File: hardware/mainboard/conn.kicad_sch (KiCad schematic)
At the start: 25 parts

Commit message: Connecting up various bits
Signed-off-by: David Shah <dave@ds0.me>
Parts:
- removed C? (x4): 10µ, symbol Device:C_Small
- removed C? (x8): 470n, symbol Device:C_Small
- removed R? (x5): 4.7k, symbol Device:R_Small
- removed U? (x8): LIFCL_40_CABGA400, symbol meowality:LIFCL_40_CABGA400
- added C? (x4): 100n, symbol Device:C_Small
- added C? (x2): 10µ, symbol Device:C_Small
- added C?: 2.2µ, symbol Device:C_Small
- added FB? (x3): 120, symbol Device:FerriteBead_Small
- added P?: M2_SOCKET_E, symbol meowality:M2_SOCKET_E
- added R?: 1.15k, symbol Device:R_Small
- added R?: 10k, symbol Device:R_Small
- added U?: LIFCL_40_CABGA400, symbol meowality:LIFCL_40_CABGA400
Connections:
- net +1V8: now also FB?.2, FB?.2
- net +3V3: now also P?.2 (3.3V), P?.4 (3.3V), P?.72 (3.3V), P?.74 (3.3V), R?.1
- net GND: now also C?.2, C?.2, C?.2, C?.2, C?.2, P?.1 (GND), P?.18 (GND), P?.33 (GND), P?.39 (GND), P?.45 (GND), P?.51 (GND), P?.57 (GND), P?.63 (GND), P?.69 (GND), P?.7 (GND), P?.75 (GND)
- new net: C?.1, C?.1, C?.1, FB?.1, U?.B13 (VCCSD0), U?.B15 (VCCSD0)
- new net: C?.1, C?.1, FB?.1, U?.B11 (VCCAUXSD)
- new net: C?.2, C?.2, FB?.1, U?.C13 (VCCPLLSD0)
- new net: R?.1, U?.C14 (SD0_REXT)
- new net: P?.55 (~PEWAKE0), R?.2
- new net +1V0: FB?.2
- new net M2_DISABLE1: P?.56 (W_DISABLE1)
- new net M2_DISABLE2: P?.54 (W_DISABLE2)
- new net M2_REFCLK0+: P?.47 (REFCLK0+)
- new net M2_REFCLK0-: P?.49 (REFCLK0-)
- new net M2_RX0+: P?.35 (PER0+), U?.A13 (SD0_TXDP/+)
- new net M2_RX0-: P?.37 (PER0-), U?.A12 (SD0_TXDN/-)
- new net M2_SDIO_CLK: P?.9 (SDIO_CLK)
- new net M2_SDIO_CMD: P?.11 (SDIO_CMD)
- new net M2_SDIO_D0: P?.13 (SDIO_D0)
- new net M2_SDIO_D1: P?.15 (SDIO_D1)
- new net M2_SDIO_D2: P?.17 (SDIO_D2)
- new net M2_SDIO_D3: P?.19 (SDIO_D3)
- new net M2_SDIO_~RESET: P?.23 (SDIO_~RESET)
- new net M2_SDIO_~WAKE: P?.21 (SDIO_~WAKE)
- new net M2_TX0+: P?.41 (PET0+), U?.A16 (SD0_RXDP/+)
- new net M2_TX0-: P?.43 (PET0-), U?.A15 (SD0_RXDN/-)
- new net M2_~RST: P?.52 (~PERST0)
- new net SD0_REFRET: C?.1, C?.1, R?.2, U?.B14 (SD0_REFRET)
- no-connect marks 0 -> 25
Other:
- note added: "1.15k --> 100Ω diff"
- note added: "Double check direction!!"

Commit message: Misc bits
Signed-off-by: David Shah <dave@ds0.me>
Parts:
- added J? (x2): Conn_01x40_Shielded, symbol Connector_Generic_Shielded:Conn_01x40_Shielded
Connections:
- net +3V3: now also J?.37 (Pin_37), J?.37 (Pin_37), J?.38 (Pin_38), J?.38 (Pin_38), J?.39 (Pin_39), J?.39 (Pin_39), J?.40 (Pin_40), J?.40 (Pin_40)
- net GND: now also J?.1 (Pin_1), J?.1 (Pin_1), J?.10 (Pin_10), J?.10 (Pin_10), J?.13 (Pin_13), J?.13 (Pin_13), J?.16 (Pin_16), J?.16 (Pin_16), J?.19 (Pin_19), J?.19 (Pin_19), J?.22 (Pin_22), J?.22 (Pin_22), J?.25 (Pin_25), J?.25 (Pin_25), J?.30 (Pin_30), J?.30 (Pin_30), J?.35 (Pin_35), J?.35 (Pin_35), J?.4 (Pin_4), J?.4 (Pin_4), J?.7 (Pin_7), J?.7 (Pin_7)
- new net B2BL_CLKI+: J?.2 (Pin_2)
- new net B2BL_CLKI-: J?.3 (Pin_3)
- new net B2BL_CLKO+: J?.8 (Pin_8)
- new net B2BL_CLKO-: J?.9 (Pin_9)
- new net B2BL_DI0+: J?.5 (Pin_5)
- new net B2BL_DI0-: J?.6 (Pin_6)
- new net B2BL_DI1+: J?.11 (Pin_11)
- new net B2BL_DI1-: J?.12 (Pin_12)
- new net B2BL_DI2+: J?.14 (Pin_14)
- new net B2BL_DI2-: J?.15 (Pin_15)
- new net B2BL_DO0+: J?.17 (Pin_17)
- new net B2BL_DO0-: J?.18 (Pin_18)
- new net B2BL_DO1+: J?.20 (Pin_20)
- new net B2BL_DO1-: J?.21 (Pin_21)
- new net B2BL_DO2+: J?.23 (Pin_23)
- new net B2BL_DO2-: J?.24 (Pin_24)
- new net B2BL_MISC0: J?.31 (Pin_31)
- new net B2BL_MISC1: J?.32 (Pin_32)
- new net B2BL_MISC2: J?.33 (Pin_33)
- new net B2BR_CLKI+: J?.14 (Pin_14), J?.8 (Pin_8)
- new net B2BR_CLKI-: J?.9 (Pin_9)
- new net B2BR_CLKO+: J?.2 (Pin_2)
- new net B2BR_CLKO-: J?.3 (Pin_3)
- new net B2BR_DI0+: J?.17 (Pin_17)
- new net B2BR_DI0-: J?.18 (Pin_18)
- new net B2BR_DI1+: J?.20 (Pin_20)
- new net B2BR_DI1-: J?.21 (Pin_21)
- new net B2BR_DI2+: J?.23 (Pin_23)
- new net B2BR_DI2-: J?.24 (Pin_24)
- new net B2BR_DO0+: J?.5 (Pin_5)
- new net B2BR_DO0-: J?.6 (Pin_6)
- new net B2BR_DO1+: J?.11 (Pin_11)
- new net B2BR_DO1-: J?.12 (Pin_12)
- new net B2BR_DO2-: J?.15 (Pin_15)
- new net B2BR_MISC0: J?.31 (Pin_31)
- new net B2BR_MISC1: J?.32 (Pin_32)
- new net B2BR_MISC2: J?.33 (Pin_33)
- new net JTAG_TCK: J?.27 (Pin_27), J?.27 (Pin_27)
- new net JTAG_TDI_L: J?.28 (Pin_28)
- new net JTAG_TDI_R: J?.28 (Pin_28)
- new net JTAG_TDO_L: J?.29 (Pin_29)
- new net JTAG_TDO_R: J?.29 (Pin_29)
- new net JTAG_TMS: J?.26 (Pin_26), J?.26 (Pin_26)
- new net PRES_L: J?.34 (Pin_34)
- new net PRES_R: J?.34 (Pin_34)
- no-connect marks 25 -> 27

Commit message: More stuff
Signed-off-by: David Shah <dave@ds0.me>
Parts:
- added C? (x2): 12p, symbol Device:C_Small
- added C? (x2): 470n, symbol Device:C_Small
- added FB?: 120R, symbol Device:FerriteBead_Small
- added J?: EAR, symbol Connector_Generic:Conn_01x06
- added R?: 10k, symbol Device:R_Small
- added U?: Si52112-B, symbol meowality:Si52112-B
- added U?: 74AHC1G126, symbol 74xGxx:74AHC1G126
- added Y?: 25MHz, symbol Device:Crystal_GND3_Small
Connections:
- net JTAG_TDO_R is gone; now on net JTAG_TDO_L: J?.29 (Pin_29)
- net +3V3: now also FB?.1, J?.1 (Pin_1), R?.2, U?.5 (VCC)
- net GND: now also J?.34 (Pin_34), C?.2, C?.2, C?.2, C?.2, J?.6 (Pin_6), U?.3 (GND), U?.4 (Vss), U?.5 (Vss), Y?.3; no longer J?.35 (Pin_35)
- net JTAG_TDI_R: now also U?.2
- net JTAG_TDO_L: now also U?.4
- net M2_REFCLK0+: now also U?.6 (DIFF1+)
- net M2_REFCLK0-: now also U?.7 (DIFF1-)
- net PRES_R: now also J?.35 (Pin_35), R?.1, U?.1; no longer J?.34 (Pin_34)
- net JTAG_TDI_L renamed JTAG_TDI
- net M2_SDIO_CLK: no longer names the net of P?.9 (SDIO_CLK)
- net M2_SDIO_CMD: no longer names the net of P?.11 (SDIO_CMD)
- net M2_SDIO_D0: no longer names the net of P?.13 (SDIO_D0)
- net M2_SDIO_D1: no longer names the net of P?.15 (SDIO_D1)
- net M2_SDIO_D2: no longer names the net of P?.17 (SDIO_D2)
- net M2_SDIO_D3: no longer names the net of P?.19 (SDIO_D3)
- net M2_SDIO_~RESET: no longer names the net of P?.23 (SDIO_~RESET)
- net M2_SDIO_~WAKE: no longer names the net of P?.21 (SDIO_~WAKE)
- new net: C?.1, C?.1, FB?.2, U?.1 (Vdd), U?.10 (Vdd)
- new net: C?.1, U?.2 (XOUT), Y?.2
- new net: C?.1, U?.3 (XIN), Y?.1
- new net EAR_0: J?.2 (Pin_2)
- new net EAR_1: J?.3 (Pin_3)
- new net EAR_2: J?.4 (Pin_4)
- new net EAR_3: J?.5 (Pin_5)
- new net NX_REFCLK+: U?.8 (DIFF2+)
- new net NX_REFCLK-: U?.9 (DIFF2-)
- no-connect marks 27 -> 43
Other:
- note added: "JTAG loop auto closed when right board not present"
- moved on the sheet: P?, R?

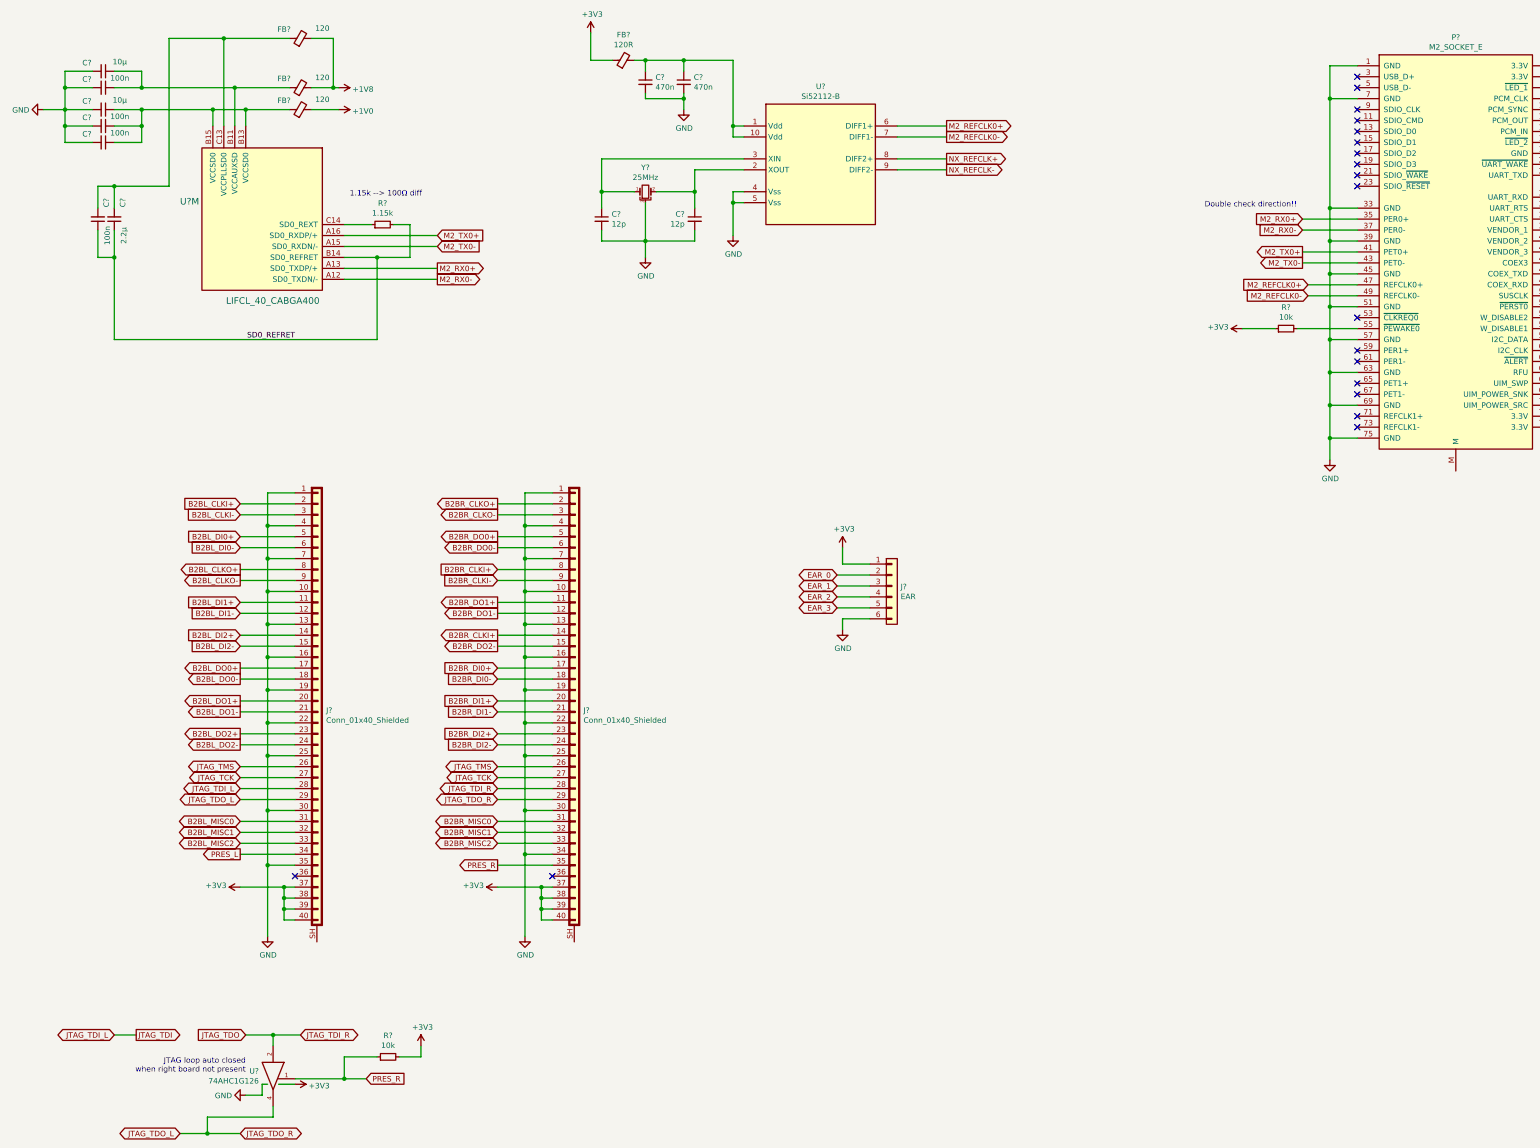
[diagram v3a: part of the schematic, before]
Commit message: Annotate and assign some footpints
Signed-off-by: David Shah <dave@ds0.me>
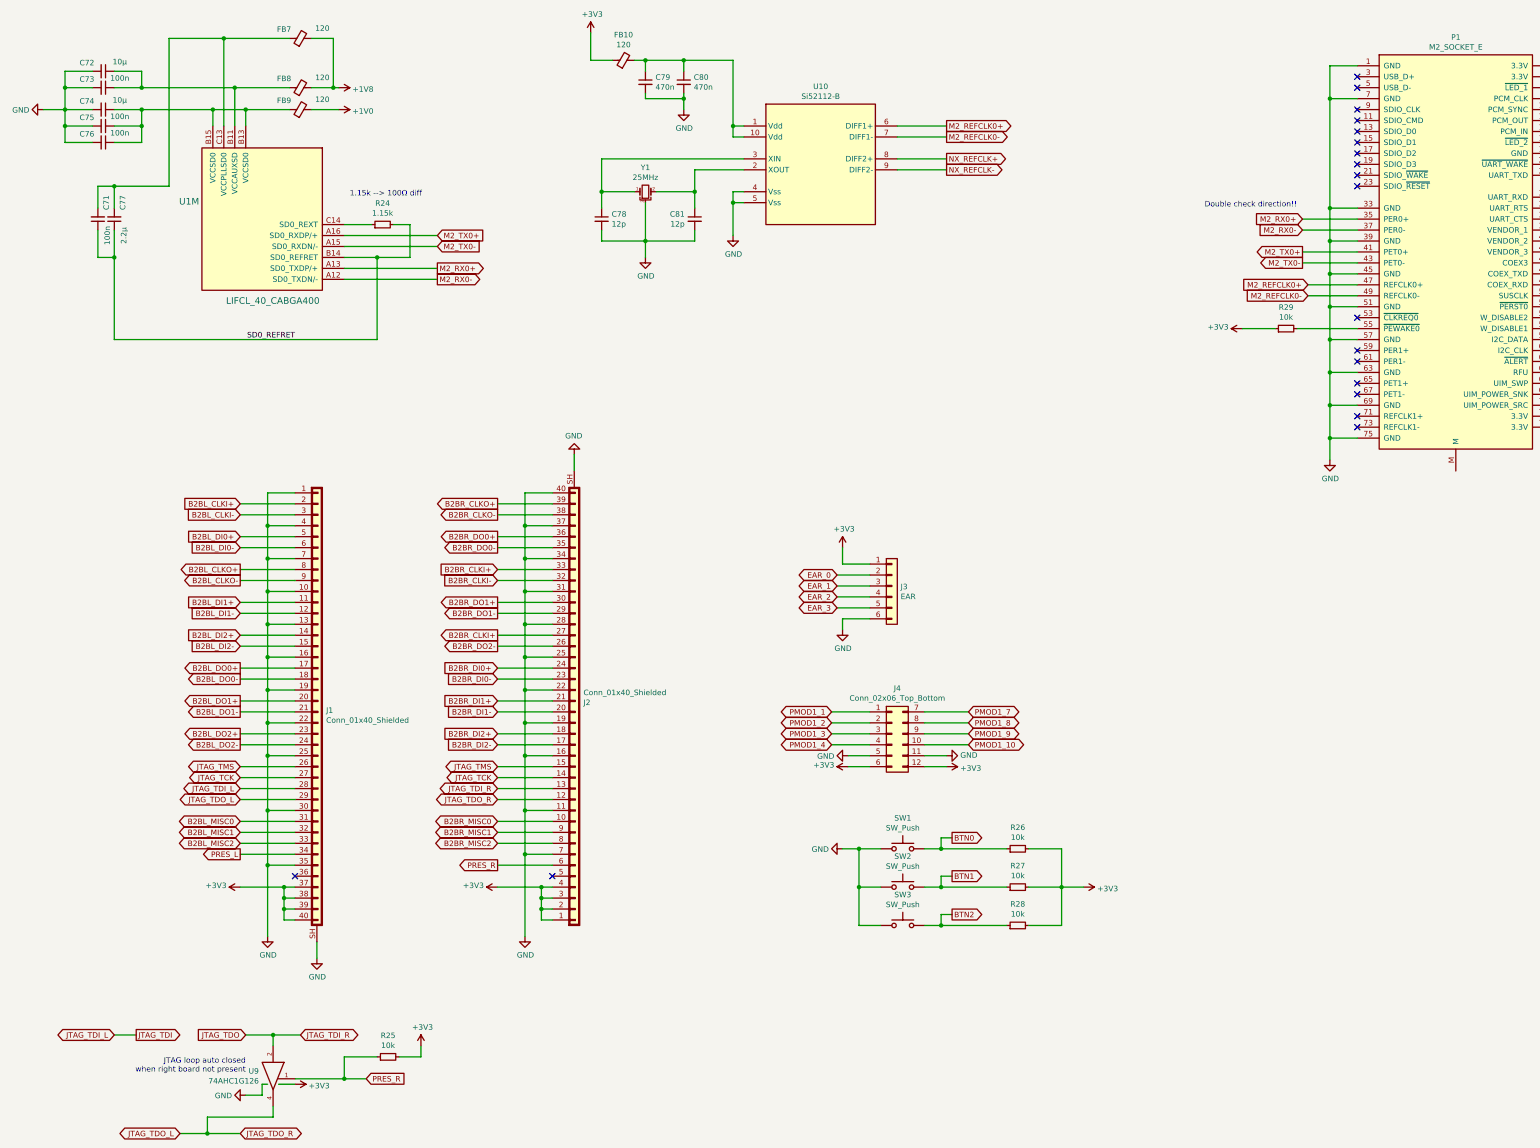
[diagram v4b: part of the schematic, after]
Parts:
- added J4: Conn_02x06_Top_Bottom, symbol Connector_Generic:Conn_02x06_Top_Bottom
- added R26, R27, R28: 10k, Resistor_SMD:R_0402_1005Metric, symbol Device:R_Small
- added SW1, SW2, SW3: SW_Push, Button_Switch_THT:SW_Tactile_SPST_Angled_PTS645Vx31-2LFS, symbol Switch:SW_Push
- C71, C73, C75, C76, C78, C79, C80, C81: renamed from C?; footprint (none) -> Capacitor_SMD:C_0402_1005Metric
- C72, C74: renamed from C?; footprint (none) -> Capacitor_SMD:C_0805_2012Metric
- C77: renamed from C?; footprint (none) -> Capacitor_SMD:C_0603_1608Metric
- FB10: renamed from FB?; value 120R -> 120; footprint (none) -> Inductor_SMD:L_0603_1608Metric
- FB7, FB8, FB9: renamed from FB?; footprint (none) -> Inductor_SMD:L_0603_1608Metric
- R24, R25, R29: renamed from R?; footprint (none) -> Resistor_SMD:R_0402_1005Metric
- U9: renamed from U?; footprint (none) -> Package_TO_SOT_SMD:SOT-23-5
- gave numbers to parts that had none: 7
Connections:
- net +3V3: now also J2.1 (Pin_1), J2.2 (Pin_2), J2.3 (Pin_3), J2.4 (Pin_4), J4.12 (Pin_12), J4.6 (Pin_6), R26.2, R27.2, R28.2; no longer J2.37 (Pin_37), J2.38 (Pin_38), J2.39 (Pin_39), J2.40 (Pin_40)
- net B2BR_CLKI+: now also J2.27 (Pin_27), J2.33 (Pin_33); no longer J2.14 (Pin_14), J2.8 (Pin_8)
- net B2BR_CLKI-: now also J2.32 (Pin_32); no longer J2.9 (Pin_9)
- net B2BR_CLKO+: now also J2.39 (Pin_39); no longer J2.2 (Pin_2)
- net B2BR_CLKO-: now also J2.38 (Pin_38); no longer J2.3 (Pin_3)
- net B2BR_DI0+: now also J2.24 (Pin_24); no longer J2.17 (Pin_17)
- net B2BR_DI0-: now also J2.23 (Pin_23); no longer J2.18 (Pin_18)
- net B2BR_DI1+: now also J2.21 (Pin_21); no longer J2.20 (Pin_20)
- net B2BR_DI1-: now also J2.20 (Pin_20); no longer J2.21 (Pin_21)
- net B2BR_DI2+: now also J2.18 (Pin_18); no longer J2.23 (Pin_23)
- net B2BR_DI2-: now also J2.17 (Pin_17); no longer J2.24 (Pin_24)
- net B2BR_DO0+: now also J2.36 (Pin_36); no longer J2.5 (Pin_5)
- net B2BR_DO0-: now also J2.35 (Pin_35); no longer J2.6 (Pin_6)
- net B2BR_DO1+: now also J2.30 (Pin_30); no longer J2.11 (Pin_11)
- net B2BR_DO1-: now also J2.29 (Pin_29); no longer J2.12 (Pin_12)
- net B2BR_DO2-: now also J2.26 (Pin_26); no longer J2.15 (Pin_15)
- net B2BR_MISC0: now also J2.10 (Pin_10); no longer J2.31 (Pin_31)
- net B2BR_MISC1: now also J2.9 (Pin_9); no longer J2.32 (Pin_32)
- net B2BR_MISC2: now also J2.8 (Pin_8); no longer J2.33 (Pin_33)
- net GND: now also J1.SH (Shield), J2.11 (Pin_11), J2.28 (Pin_28), J2.31 (Pin_31), J2.37 (Pin_37), J2.40 (Pin_40), J2.SH (Shield), J4.11 (Pin_11), J4.5 (Pin_5), SW1.1, SW2.1, SW3.1; no longer J2.1 (Pin_1), J2.10 (Pin_10), J2.13 (Pin_13), J2.30 (Pin_30), J2.4 (Pin_4)
- net JTAG_TCK: now also J2.14 (Pin_14); no longer J2.27 (Pin_27)
- net JTAG_TDI_R: now also J2.13 (Pin_13); no longer J2.28 (Pin_28)
- net JTAG_TDO_L: now also J2.12 (Pin_12); no longer J2.29 (Pin_29)
- net JTAG_TMS: now also J2.15 (Pin_15); no longer J2.26 (Pin_26)
- net PRES_R: now also J2.6 (Pin_6); no longer J2.35 (Pin_35)
- new net BTN0: R26.1, SW1.2
- new net BTN1: R27.1, SW2.2
- new net BTN2: R28.1, SW3.2
- new net PMOD1_1: J4.1 (Pin_1)
- new net PMOD1_10: J4.10 (Pin_10)
- new net PMOD1_2: J4.2 (Pin_2)
- new net PMOD1_3: J4.3 (Pin_3)
- new net PMOD1_4: J4.4 (Pin_4)
- new net PMOD1_7: J4.7 (Pin_7)
- new net PMOD1_8: J4.8 (Pin_8)
- new net PMOD1_9: J4.9 (Pin_9)
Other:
- moved on the sheet: J2

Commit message: Add and assign more footprints
Signed-off-by: David Shah <dave@ds0.me>
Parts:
- J1, J2: footprint (none) -> meowality:TE_FPC_40pin_p0.5mm_4-1734839-0
- J3: footprint (none) -> Connector_PinHeader_2.54mm:PinHeader_2x03_P2.54mm_Horizontal
- J4: footprint (none) -> Connector_PinSocket_2.54mm:PinSocket_2x06_P2.54mm_Horizontal
- P1: footprint (none) -> meowality:2199230-4
- U1: footprint (none) -> meowality:BGA-400_20x20_17.0x17.0mm
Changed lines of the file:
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@@
       (effects (font (size 1.27 1.27)) (justify left))
     )
-    (property "Footprint" "" (id 2) (at 220.98 148.59 0)
+    (property "Footprint" "Connector_PinHeader_2.54mm:PinHeader_2x03_P2.54mm_Horizontal" (id 2) (at 220.98 148.59 0)
       (effects (font (size 1.27 1.27)) hide)
     )
@@
     (property "Reference" "J4" (id 0) (at 222.25 172.3198 0))
     (property "Value" "Conn_02x06_Top_Bottom" (id 1) (at 222.25 174.6185 0))
-    (property "Footprint" "" (id 2) (at 220.98 182.88 0)
+    (property "Footprint" "Connector_PinSocket_2.54mm:PinSocket_2x06_P2.54mm_Horizontal" (id 2) (at 220.98 182.88 0)
       (effects (font (size 1.27 1.27)) hide)
     )
@@
       (effects (font (size 1.27 1.27)) (justify left))
     )
-    (property "Footprint" "" (id 2) (at 87.63 175.26 0)
+    (property "Footprint" "meowality:TE_FPC_40pin_p0.5mm_4-1734839-0" (id 2) (at 87.63 175.26 0)
       (effects (font (size 1.27 1.27)) hide)
     )
@@
       (effects (font (size 1.27 1.27)) (justify left))
     )
-    (property "Footprint" "" (id 2) (at 147.32 177.8 0)
+    (property "Footprint" "meowality:TE_FPC_40pin_p0.5mm_4-1734839-0" (id 2) (at 147.32 177.8 0)
       (effects (font (size 1.27 1.27)) hide)
     )
@@
       (effects (font (size 1.524 1.524)) (justify left))
     )
-    (property "Footprint" "" (id 2) (at 90.17 63.5 0)
+    (property "Footprint" "meowality:BGA-400_20x20_17.0x17.0mm" (id 2) (at 90.17 63.5 0)
       (effects (font (size 1.524 1.524)) (justify right) hide)
     )
@@
     (property "Reference" "P1" (id 0) (at 351.79 21.3168 0))
     (property "Value" "M2_SOCKET_E" (id 1) (at 351.79 23.6155 0))
-    (property "Footprint" "" (id 2) (at 351.79 44.45 0)
-      (effects (font (size 1.27 1.27)) hide)
-    )
+    (property "Footprint" "meowality:2199230-4" (id 2) (at 351.79 44.45 0)
+      (effects (font (size 1.27 1.27)) hide)
+    )

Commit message: First pass at placement
Signed-off-by: David Shah <dave@ds0.me>
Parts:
- U10: footprint (none) -> meowality:TDFN10_3x3mm_p0.5mm
- Y1: footprint (none) -> Crystal:Crystal_SMD_2016-4Pin_2.0x1.6mm; symbol Device:Crystal_GND3_Small -> Device:Crystal_GND24_Small
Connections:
- net GND: now also U10.11 (Vss), Y1.2, Y1.4; no longer Y1.3
- net at C81.1, U10.2 (XOUT): now also Y1.3; no longer Y1.2
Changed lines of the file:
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@@
   (junction (at 153.67 57.15) (diameter 1.016) (color 0 0 0 0))
   (junction (at 163.83 26.67) (diameter 1.016) (color 0 0 0 0))
+  (junction (at 163.83 60.96) (diameter 1.016) (color 0 0 0 0))
   (junction (at 163.83 68.58) (diameter 1.016) (color 0 0 0 0))
   (junction (at 172.72 26.67) (diameter 1.016) (color 0 0 0 0))
@@
   (junction (at 184.15 41.91) (diameter 1.016) (color 0 0 0 0))
   (junction (at 184.15 59.69) (diameter 1.016) (color 0 0 0 0))
+  (junction (at 184.15 62.23) (diameter 1.016) (color 0 0 0 0))
   (junction (at 213.36 209.55) (diameter 1.016) (color 0 0 0 0))
   (junction (at 213.36 218.44) (diameter 1.016) (color 0 0 0 0))
@@
     (stroke (width 0) (type solid) (color 0 0 0 0))
   )
-  (wire (pts (xy 163.83 59.69) (xy 163.83 68.58))
+  (wire (pts (xy 163.83 53.34) (xy 168.91 53.34))
+    (stroke (width 0) (type solid) (color 0 0 0 0))
+  )
+  (wire (pts (xy 163.83 54.61) (xy 163.83 53.34))
+    (stroke (width 0) (type solid) (color 0 0 0 0))
+  )
+  (wire (pts (xy 163.83 59.69) (xy 163.83 60.96))
+    (stroke (width 0) (type solid) (color 0 0 0 0))
+  )
+  (wire (pts (xy 163.83 60.96) (xy 163.83 68.58))
     (stroke (width 0) (type solid) (color 0 0 0 0))
   )
@@
     (stroke (width 0) (type solid) (color 0 0 0 0))
   )
+  (wire (pts (xy 168.91 53.34) (xy 168.91 60.96))
+    (stroke (width 0) (type solid) (color 0 0 0 0))
+  )
+  (wire (pts (xy 168.91 60.96) (xy 163.83 60.96))
+    (stroke (width 0) (type solid) (color 0 0 0 0))
+  )
   (wire (pts (xy 172.72 26.67) (xy 172.72 29.21))
     (stroke (width 0) (type solid) (color 0 0 0 0))
@@
     (stroke (width 0) (type solid) (color 0 0 0 0))
   )
-  (wire (pts (xy 184.15 67.31) (xy 184.15 59.69))
+  (wire (pts (xy 184.15 62.23) (xy 184.15 59.69))
+    (stroke (width 0) (type solid) (color 0 0 0 0))
+  )
+  (wire (pts (xy 184.15 62.23) (xy 186.69 62.23))
+    (stroke (width 0) (type solid) (color 0 0 0 0))
+  )
+  (wire (pts (xy 184.15 67.31) (xy 184.15 62.23))
     (stroke (width 0) (type solid) (color 0 0 0 0))
   )
@@
     (pin "2")
   )
-  (symbol (lib_id "Device:Crystal_GND3_Small") (at 163.83 57.15 0) (unit 1)
+  (symbol (lib_id "Device:Crystal_GND24_Small") (at 163.83 57.15 0) (unit 1)
     (in_bom yes) (on_board yes)
     (property "Reference" "Y1" (id 0) (at 163.83 51.5428 0))
     (property "Value" "25MHz" (id 1) (at 163.83 53.841 0))
-    (property "Footprint" "" (id 2) (at 163.83 57.15 0)
+    (property "Footprint" "Crystal:Crystal_SMD_2016-4Pin_2.0x1.6mm" (id 2) (at 163.83 57.15 0)
       (effects (font (size 1.27 1.27)) hide)
     )
@@
     (pin "2")
     (pin "3")
+    (pin "4")
   )
   (symbol (lib_id "Switch:SW_Push") (at 223.52 209.55 0) (unit 1)
@@
     (property "Reference" "U10" (id 0) (at 204.47 32.7463 0))
     (property "Value" "Si52112-B" (id 1) (at 204.47 35.045 0))
-    (property "Footprint" "" (id 2) (at 204.47 64.77 0)
+    (property "Footprint" "meowality:TDFN10_3x3mm_p0.5mm" (id 2) (at 204.47 64.77 0)
       (effects (font (size 1.27 1.27)) hide)
     )
@@
     (pin "8")
     (pin "9")
+    (pin "11")
   )
   (symbol (lib_id "meowality:LIFCL_40_CABGA400") (at 93.98 64.77 0) (mirror y) (unit 13)
